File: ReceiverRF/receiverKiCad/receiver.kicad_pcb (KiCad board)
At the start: 2 copper layers, 95.4 x 60 mm, 74 parts, among them J1 Conn_Coaxial, J2 Conn_01x05_Socket, J3 Conn_01x04, Q1 MMBT3904, SW1 SW_Push, SW2 SW_Push, SW3 SW_Push, SW4 SW_Push, SW5 SW_SPST, U1 STM32F103RET6, U2 NCV5501DT33RKG, U3 NJM2882F05-TE1, U4 MLX90393SLW-ABA-011-RE, Y1 Crystal_GND24

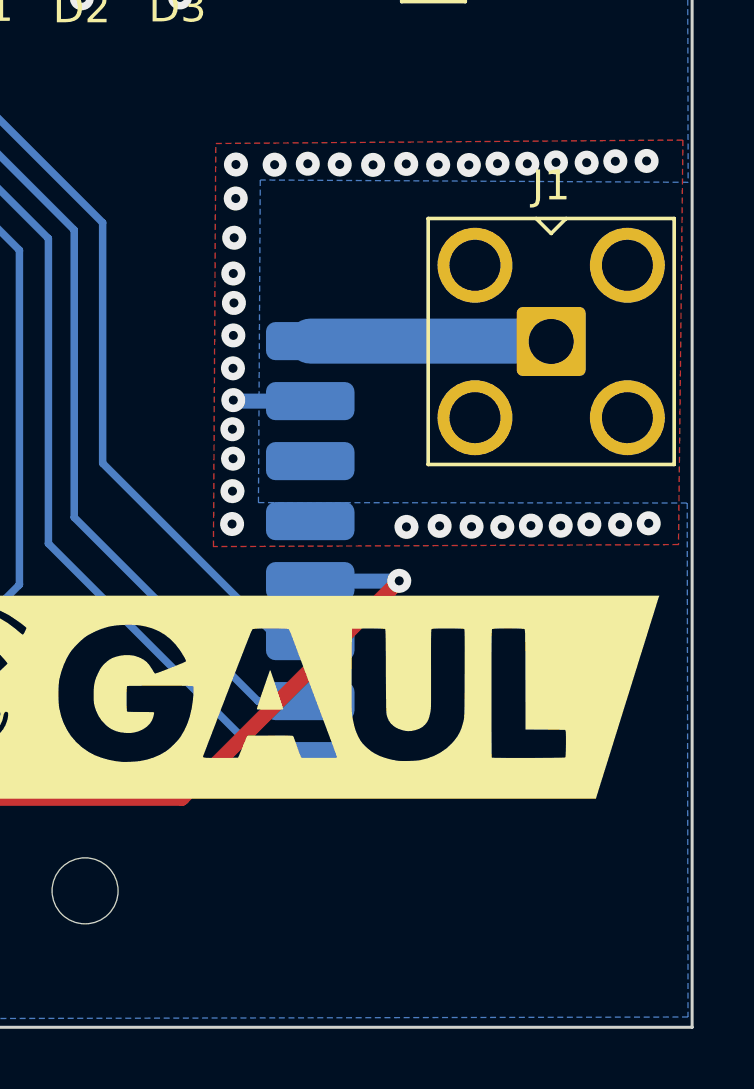
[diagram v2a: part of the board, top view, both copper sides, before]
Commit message: impédance 50 ohm pour l'Antenne
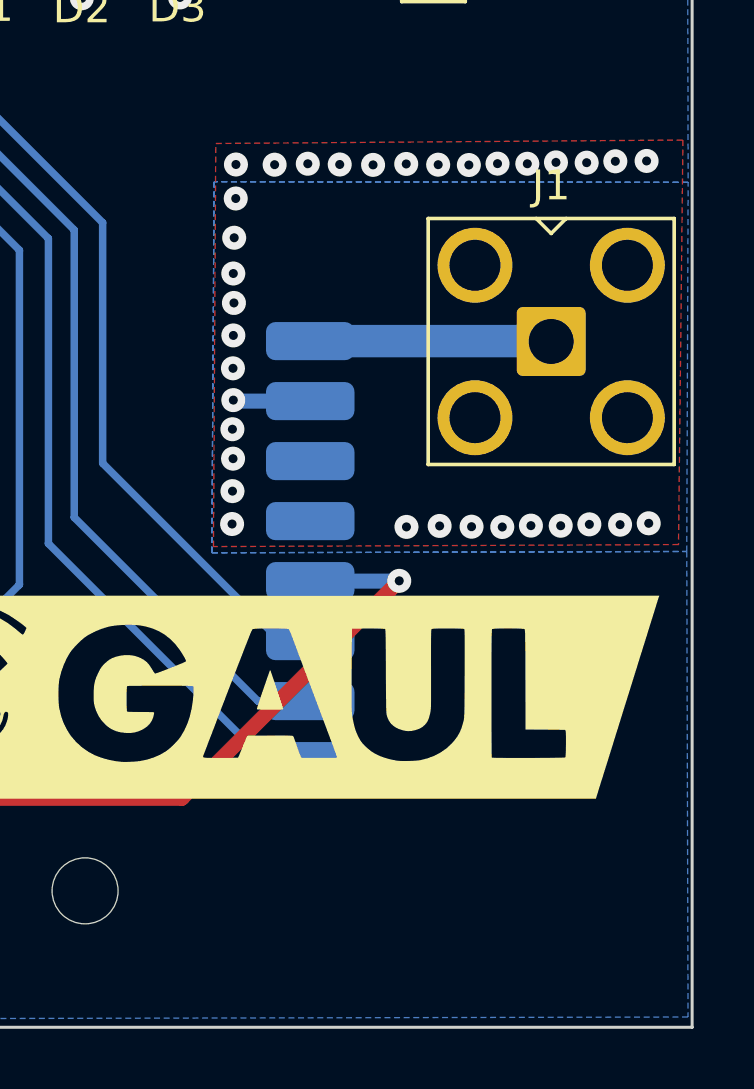
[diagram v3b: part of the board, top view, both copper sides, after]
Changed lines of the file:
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@@
 		(tags "SOD-123")
 		(property "Reference" "BUZ_D1"
-			(at -0.233455 2.016688 360)
+			(at -0.233455 2.016688 0)
 			(layer "F.SilkS")
 			(effects
@@
 		)
 		(property "Value" "~"
-			(at 0 2.1 360)
+			(at 0 2.1 0)
 			(layer "F.Fab")
 			(effects
@@
 		(tags "resistor")
 		(property "Reference" "BUZ_R2"
-			(at -1.722742 -1.303791 360)
+			(at -1.722742 -1.303791 0)
 			(layer "F.SilkS")
 			(effects
@@
 		)
 		(property "Value" "1k5"
-			(at 0 1.17 360)
+			(at 0 1.17 0)
 			(layer "F.Fab")
 			(hide yes)
@@
 		)
 		(fp_text user "${REFERENCE}"
-			(at 0 0 360)
+			(at 0 0 0)
 			(layer "F.Fab")
 			(effects
@@
 	)
 	(segment
-		(start 190.487388 116.827388)
-		(end 190.5 116.84)
-		(width 0.25)
+		(start 182.468615 116.827388)
+		(end 190.487388 116.827388)
+		(width 1.08216)
 		(layer "B.Cu")
 		(net 19)
 	)
 	(segment
-		(start 182.468615 116.827388)
-		(end 190.487388 116.827388)
-		(width 1.5)
+		(start 190.487388 116.827388)
+		(end 190.5 116.84)
+		(width 1.08216)
 		(layer "B.Cu")
 		(net 19)
@@
 		(layer "F.Cu")
 		(hatch edge 0.5)
-		(connect_pads
+		(connect_pads yes
 			(clearance 0.5)
 		)
@@
 		(polygon
 			(pts
-				(xy 100.067449 80.031766) (xy 194.996184 79.843388) (xy 195.065676 111.533744) (xy 180.803404 111.456991)
-				(xy 180.7424 122.210629) (xy 195.03413 122.223925) (xy 195.062364 139.357382) (xy 100.046468 139.561761)
+				(xy 100.067449 80.031766) (xy 194.996184 79.843388) (xy 195.065676 111.533744) (xy 179.26497 111.514686)
+				(xy 179.1891 123.883809) (xy 195.019264 123.83941) (xy 195.062364 139.357382) (xy 100.046468 139.561761)
+			)
+		)
+	)
+	(zone
+		(net 1)
+		(net_name "GND")
+		(layer "B.Cu")
+		(hatch edge 0.5)
+		(priority 2)
+		(connect_pads yes
+			(clearance 0.2)
+		)
+		(min_thickness 0.25)
+		(filled_areas_thickness no)
+		(fill yes
+			(thermal_gap 0.5)
+			(thermal_bridge_width 0.5)
+		)
+		(polygon
+			(pts
+				(xy 195.065676 111.533744) (xy 179.26497 111.514686) (xy 179.1891 123.883809) (xy 195.019264 123.83941)
 			)
 		)

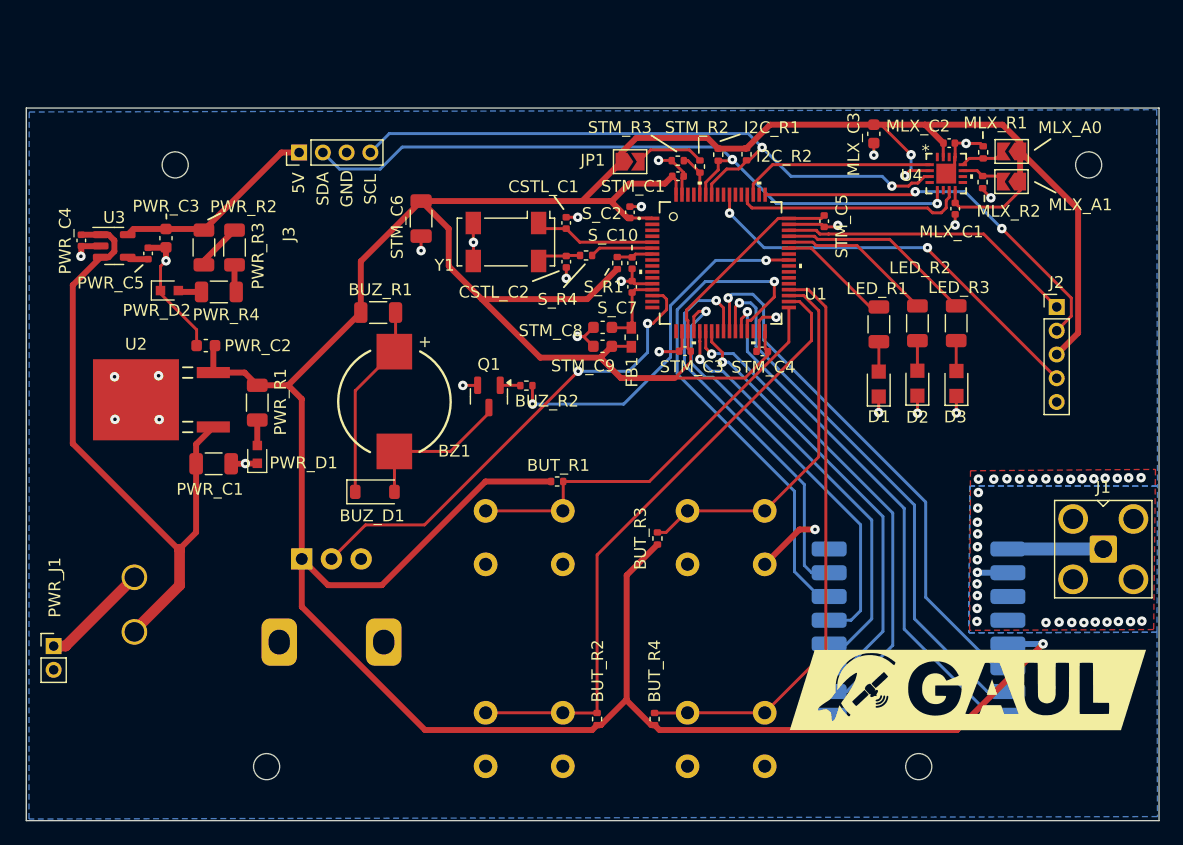
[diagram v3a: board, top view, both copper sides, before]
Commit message: copper pour sur top layer et amélioration coplanar waveguide pour trace RF
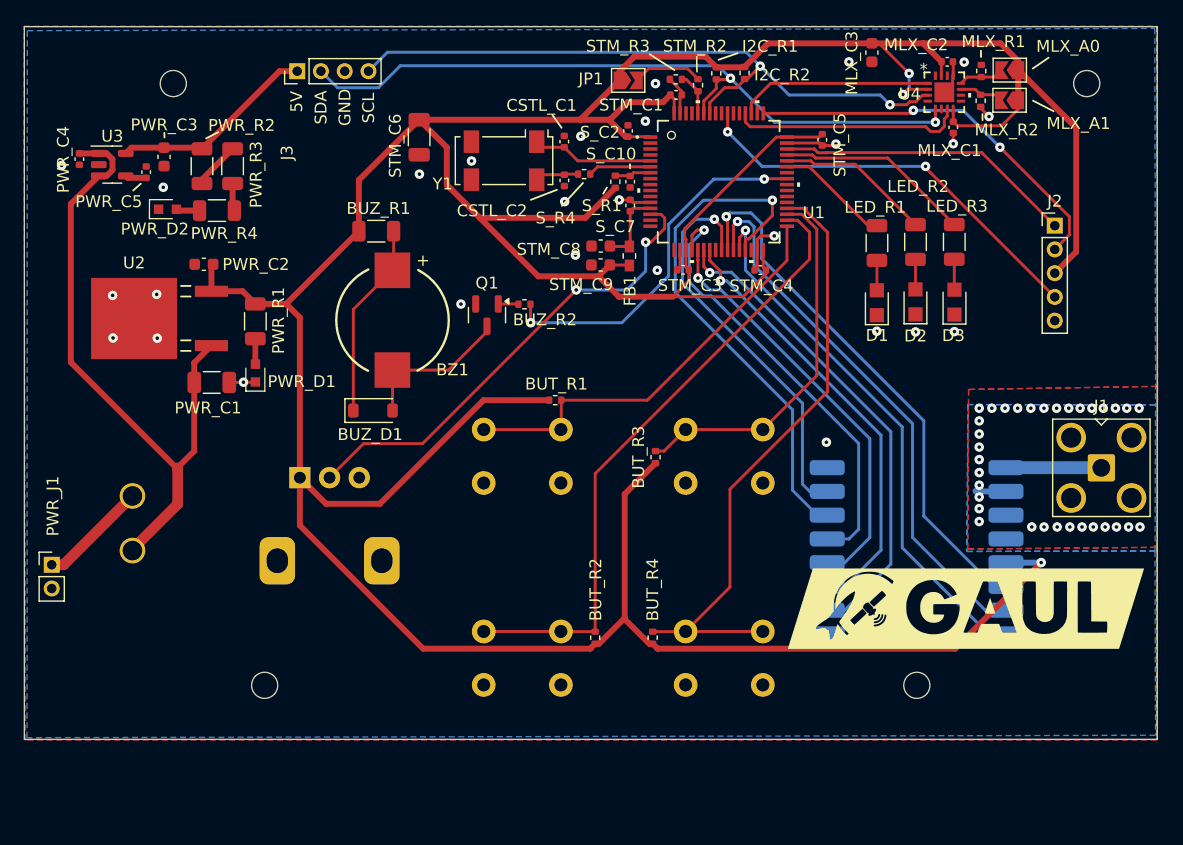
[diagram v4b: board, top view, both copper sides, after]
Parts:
- moved BUT_R2 6.85 mm to (147.7, 124.3)
- moved BUT_R4 6.85 mm to (152.6, 124.3)
- moved G*** 6.85 mm to (178.9, 121.8)
- moved REF** 6.85 mm to (119.9, 128.3)
- moved REF** 6.85 mm to (174.8, 128.3)
- moved MLX_A0 6.85 mm to (182.6, 76.5)
- moved MLX_R1 6.85 mm to (180.2, 76.6)
- moved STM_C9 6.85 mm to (148.2, 92.9)
- moved STM_R2 6.85 mm to (156.4, 77.8)
- moved STM_R3 6.85 mm to (154.5, 77.3)
- moved S_C7 6.85 mm to (150.7, 87.9)
- moved BUT_R1 6.85 mm to (144.4, 104.3)
- moved BUT_R3 6.85 mm to (152.8, 109.1)
- moved BUZ_R1 6.85 mm to (129.3, 90.1)
- moved BZ1 6.85 mm to (130.6, 97.6)
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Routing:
- net GND: track 68.3 -> 26.6 mm, vias 61 -> 60
- net PUSH_4: track 49.3 -> 52.3 mm
